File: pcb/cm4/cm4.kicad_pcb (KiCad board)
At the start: 4 copper layers, 86.4 x 55.9 mm, 30 parts, among them J101 Conn_01x05, J102 Conn_01x08, J201 DF40C-100DS-0.4V_51_, J202 DF40C-100DS-0.4V_51_, J301 HR911130A, J401 Micro_SD_Card, U201 SN74LV1T34DBV, U301 TPD4EUSB30, U302 TPD4EUSB30, U401 RT9742GGJ5

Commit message: update cm4 board
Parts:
- removed J401: Micro_SD_Card, Connector_Card:microSD_HC_Wuerth_693072010801
- added MICRO_SD401: TF-01A, DF40C-100DS-0.4V_51_:TF-01A, F.Cu at (84.7, 94.5)
- moved R301 13.9 mm to (100.2, 103.7)
- moved C301 6.71 mm to (100.0, 107.2), turned to -90 degrees

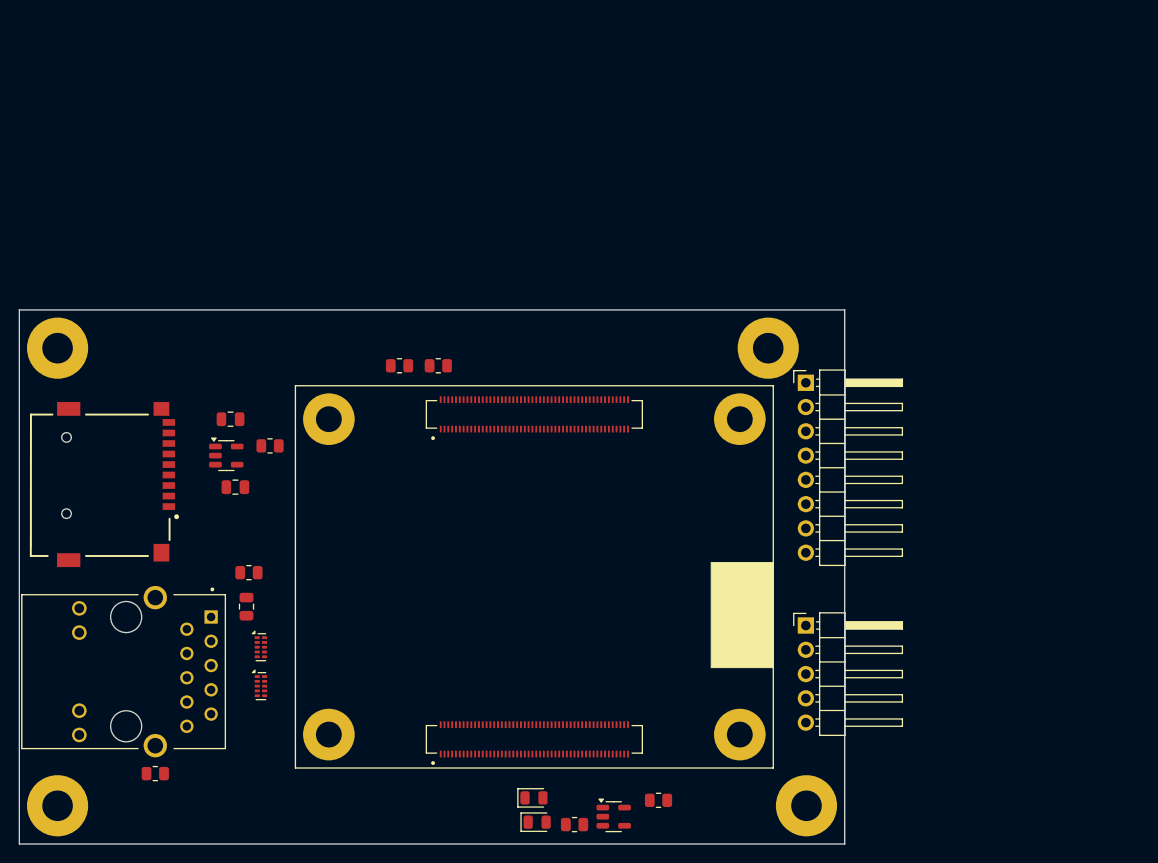
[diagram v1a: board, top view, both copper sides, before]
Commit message: cm4: update footprint library, add 3d files, update dimensions
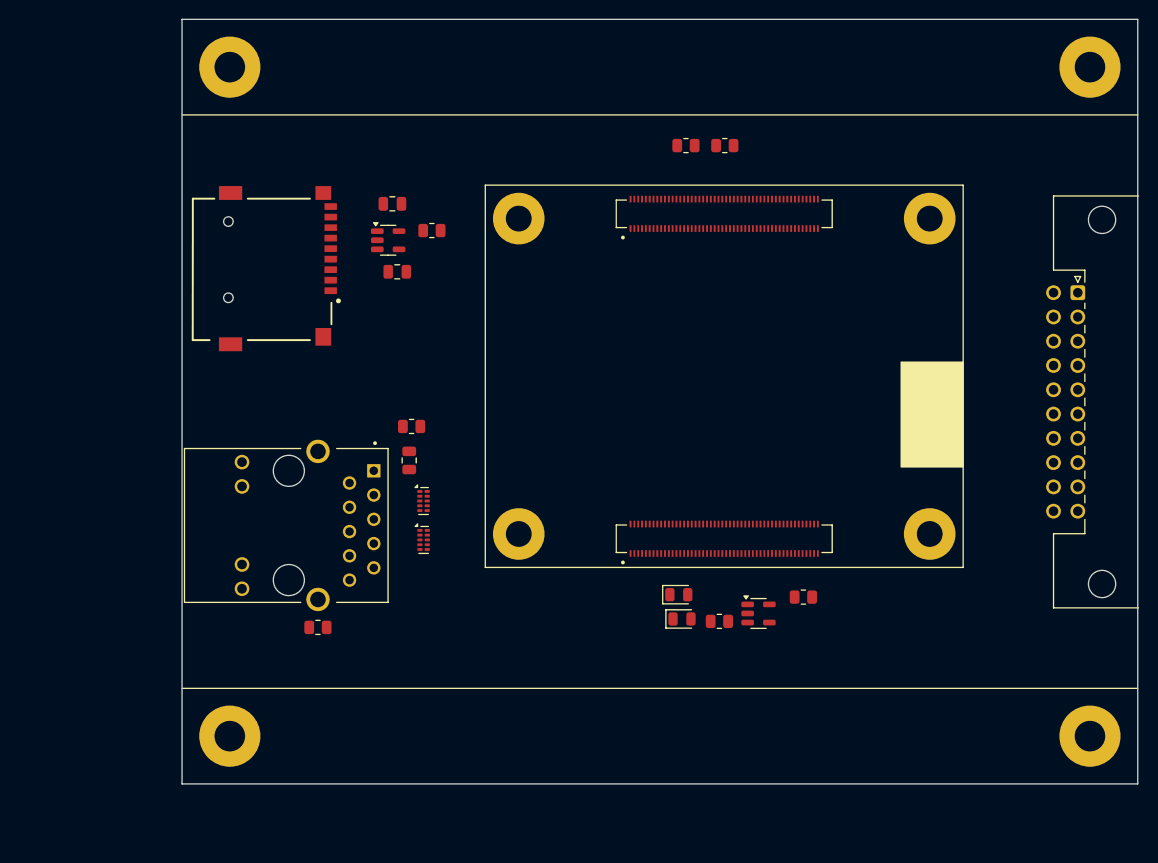
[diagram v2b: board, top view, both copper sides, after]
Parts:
- removed J102: Conn_01x08, Connector_PinHeader_2.54mm:PinHeader_1x08_P2.54mm_Horizontal
- J101: value Conn_01x05 -> Conn_02x10_Row_Letter_First; footprint Connector_PinHeader_2.54mm:PinHeader_1x05_P2.54mm_Horizontal -> PRJ:PCN10C-20S-2.54DS
- J201, J202: footprint DF40C-100DS-0.4V_51_:HIROSE_DF40C-100DS-0.4V_51_ -> PRJ:HIROSE_DF40C-100DS-0.4V_51_
- J301: footprint DF40C-100DS-0.4V_51_:HANRUN_HR911130A -> PRJ:HANRUN_HR911130A
- MICRO_SD401: footprint DF40C-100DS-0.4V_51_:TF-01A -> PRJ:TF-01A
- moved J101 45.0 mm to (186.9, 74.4), turned to -90 degrees
- moved REF** 44.7 mm to (188.2, 50.8)
- moved R202 37.8 mm to (150.0, 59.0)
- moved R203 37.8 mm to (146.0, 59.0)
- moved REF** 34.5 mm to (98.2, 50.8)
- moved REF** 30.5 mm to (188.2, 120.8)
- moved REF** 28.9 mm to (128.5, 99.6)
- moved REF** 28.9 mm to (128.5, 66.6)
- moved J201 28.9 mm to (150.0, 100.1)
- moved J202 28.9 mm to (150.0, 66.1)
- moved REF** 28.9 mm to (171.5, 66.6)
- moved REF** 28.9 mm to (171.5, 99.6)
- moved MICRO_SD401 28.2 mm to (101.6, 72.0)
- moved R401 28.2 mm to (119.4, 67.9)
- moved C401 28.2 mm to (115.7, 72.2)
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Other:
- board size 86.4 x 55.9 mm -> 100 x 80 mm

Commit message: update
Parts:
- moved R201 9.66 mm to (148.8, 108.5), turned to 180 degrees
- moved D202 9.57 mm to (154.7, 111.3)
- moved R203 9.39 mm to (137.2, 62.3)
- moved R202 9.39 mm to (141.2, 62.3)
- moved U201 6.62 mm to (160.0, 109.3), turned to -90 degrees
- moved R301 6.56 mm to (110.7, 87.5)
- moved D201 6.46 mm to (148.8, 111.3), turned to 180 degrees
- moved R204 5.25 mm to (154.7, 108.5)
- moved J201 2.72 mm to (150.9, 102.7)
- moved J202 2.72 mm to (150.9, 68.7)
- moved REF** 2.72 mm to (172.4, 69.2)
- moved REF** 2.72 mm to (129.4, 102.2)
- moved REF** 2.72 mm to (172.4, 102.2)
- moved REF** 2.72 mm to (129.4, 69.2)
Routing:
- net +5V: track 0.00 -> 10.2 mm
- net +12V: track 0.00 -> 10.2 mm

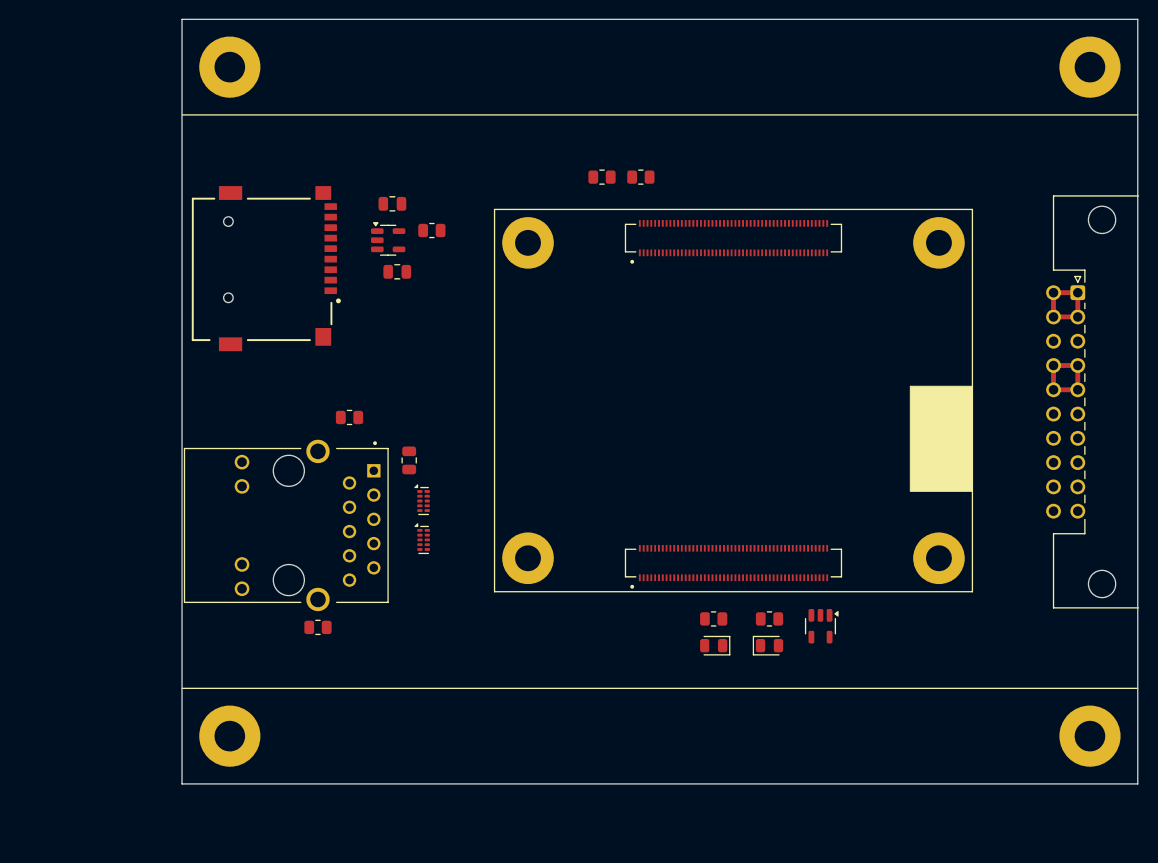
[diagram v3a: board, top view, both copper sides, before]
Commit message: finish all routing
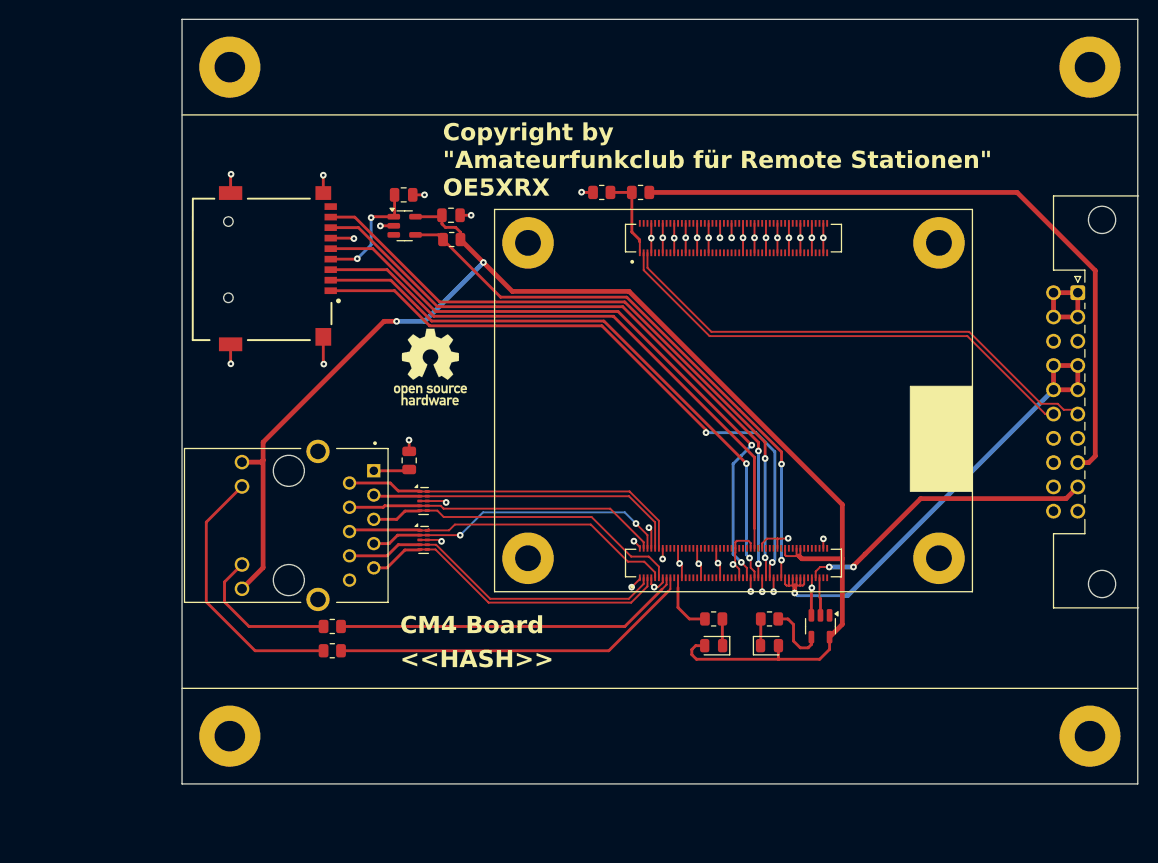
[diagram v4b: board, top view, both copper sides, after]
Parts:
- added #SYM101: OSHW-Logo_7.5x8mm_SilkScreen, Symbol:OSHW-Logo_7.5x8mm_SilkScreen, F.Cu at (119.2, 82.2)
- moved R301 24.5 mm to (108.9, 111.9)
- moved C401 8.16 mm to (121.4, 66.3)
- moved U401 2.29 mm to (116.5, 67.4)
- moved R401 2.28 mm to (121.4, 68.8), turned to 180 degrees
- moved R202 1.60 mm to (141.2, 63.9)
- moved R203 1.60 mm to (137.1, 63.9)
- moved C402 1.51 mm to (116.4, 64.2)
- moved R302 1.50 mm to (108.9, 109.3)
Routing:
- net +3V3: track 0.00 -> 150.1 mm, vias 0 -> 2
- net GND: track 0.00 -> 107.2 mm, vias 0 -> 43
- net /USB_OTG_ID: track 0.00 -> 71.6 mm
- net /CM4-Board/SD_DATA1: track 0.00 -> 69.4 mm, vias 0 -> 2
- net /CM4-Board/SD_DATA0: track 0.00 -> 68.2 mm, vias 0 -> 2
- net /CM4-Board/SD_CLK: track 0.00 -> 67.9 mm, vias 0 -> 2
- net /CM4-Board/SD_DATA2: track 0.00 -> 67.0 mm, vias 0 -> 2
- net /CM4-Board/SD_DATA3: track 0.00 -> 63.7 mm, vias 0 -> 2
- net /CM4-Board/SD_CMD: track 0.00 -> 62.0 mm
- net /CM4-Board/SD_PWR_ON: track 0.00 -> 60.9 mm, vias 0 -> 2
- net /USB+: track 0.00 -> 52.9 mm
- net /USB-: track 0.00 -> 50.9 mm
- net +5V: track 10.2 -> 53.8 mm, vias 0 -> 1
- net /CM4-Board/ETH_GREEN: track 0.00 -> 38.3 mm
- net /CM4-Board/TRD0+: track 0.00 -> 36.9 mm
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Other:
- board text added: "<<HASH>>"
- board text added: "CM4 Board"
- board text added: "Copyright by {dblquote}Amateurfunkclub für Remote Stationen{dblquote} OE5XRX"

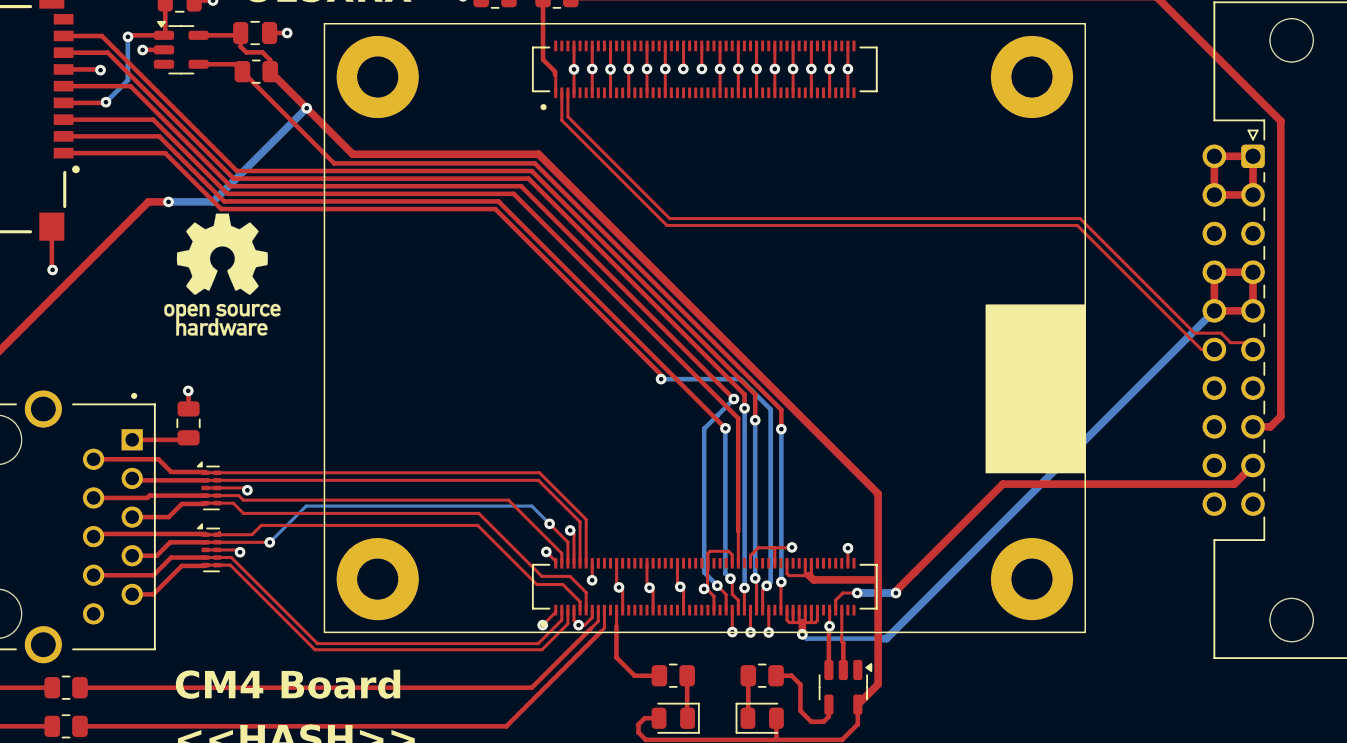
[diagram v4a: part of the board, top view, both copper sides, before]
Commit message: update diff pairs
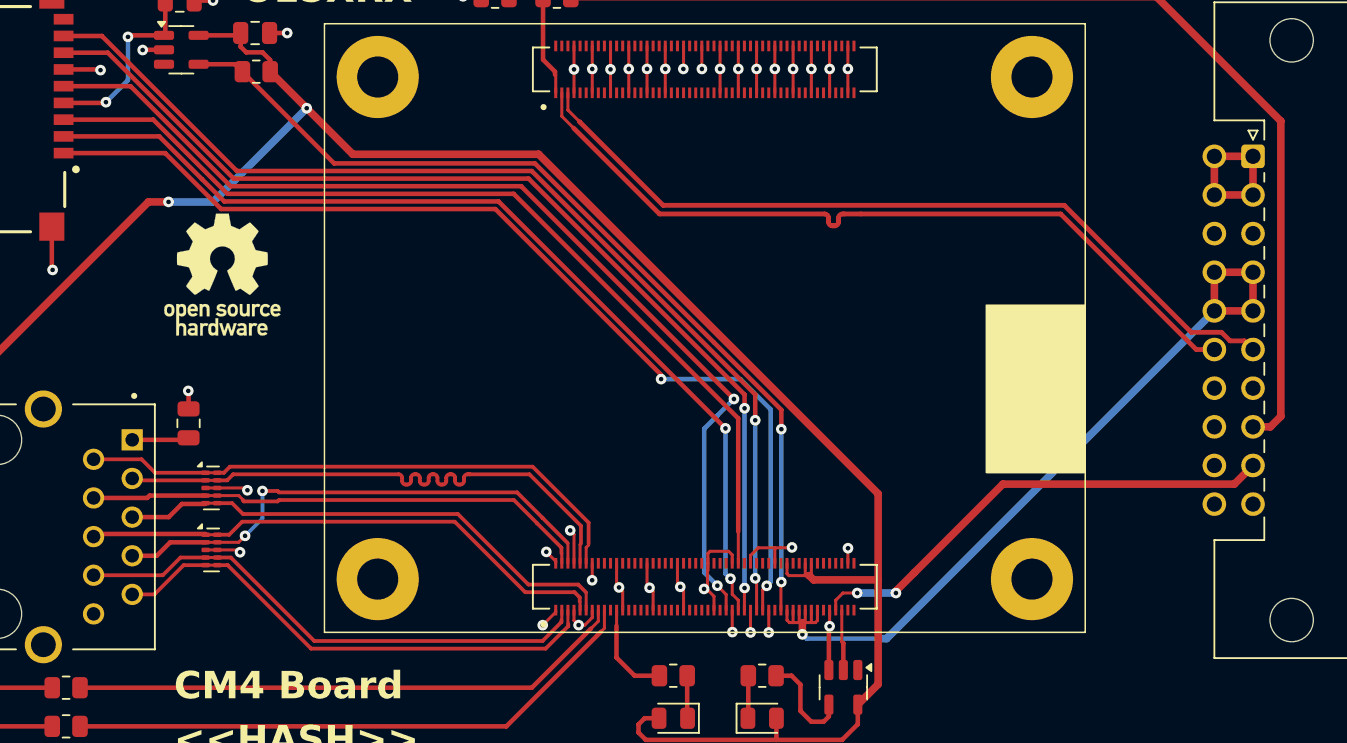
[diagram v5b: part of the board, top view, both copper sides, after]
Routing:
- net /CM4-Board/TRD0-: track 33.3 -> 37.4 mm
- net /CM4-Board/TRD1-: track 32.4 -> 34.2 mm
- net /USB-: track 50.9 -> 51.8 mm

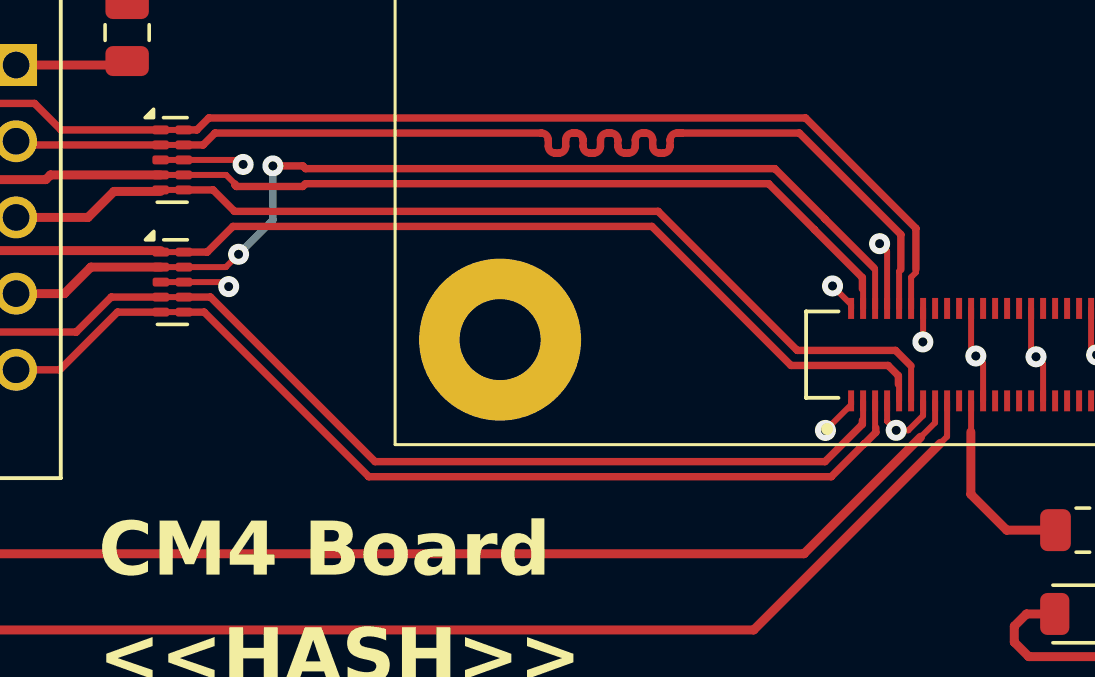
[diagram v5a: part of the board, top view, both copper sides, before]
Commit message: fix diff pairs
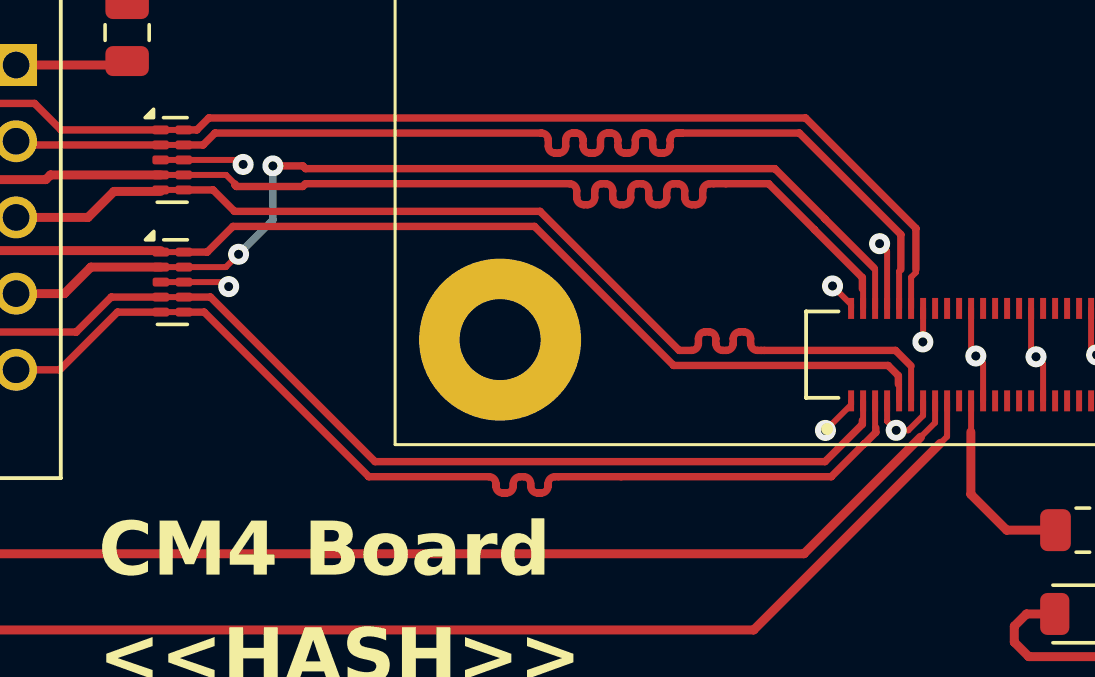
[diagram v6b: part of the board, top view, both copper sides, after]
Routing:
- net /CM4-Board/TRD1+: track 33.4 -> 37.2 mm
- net /CM4-Board/TRD2+: track 33.8 -> 35.4 mm
- net /CM4-Board/TRD3-: track 33.4 -> 34.7 mm
